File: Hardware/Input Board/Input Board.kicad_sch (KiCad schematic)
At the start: 13 parts, among them J1 Keyboard, J2 Mouse, J3 PORT A, J4 Audio L, J5 Audio R, J6 3.5mm TRS, J7 SNES Controller 1, J8 PORT B, J9 SNES Controller 2, U1 74HC595, U2 Adafruit MicroSD Breakout

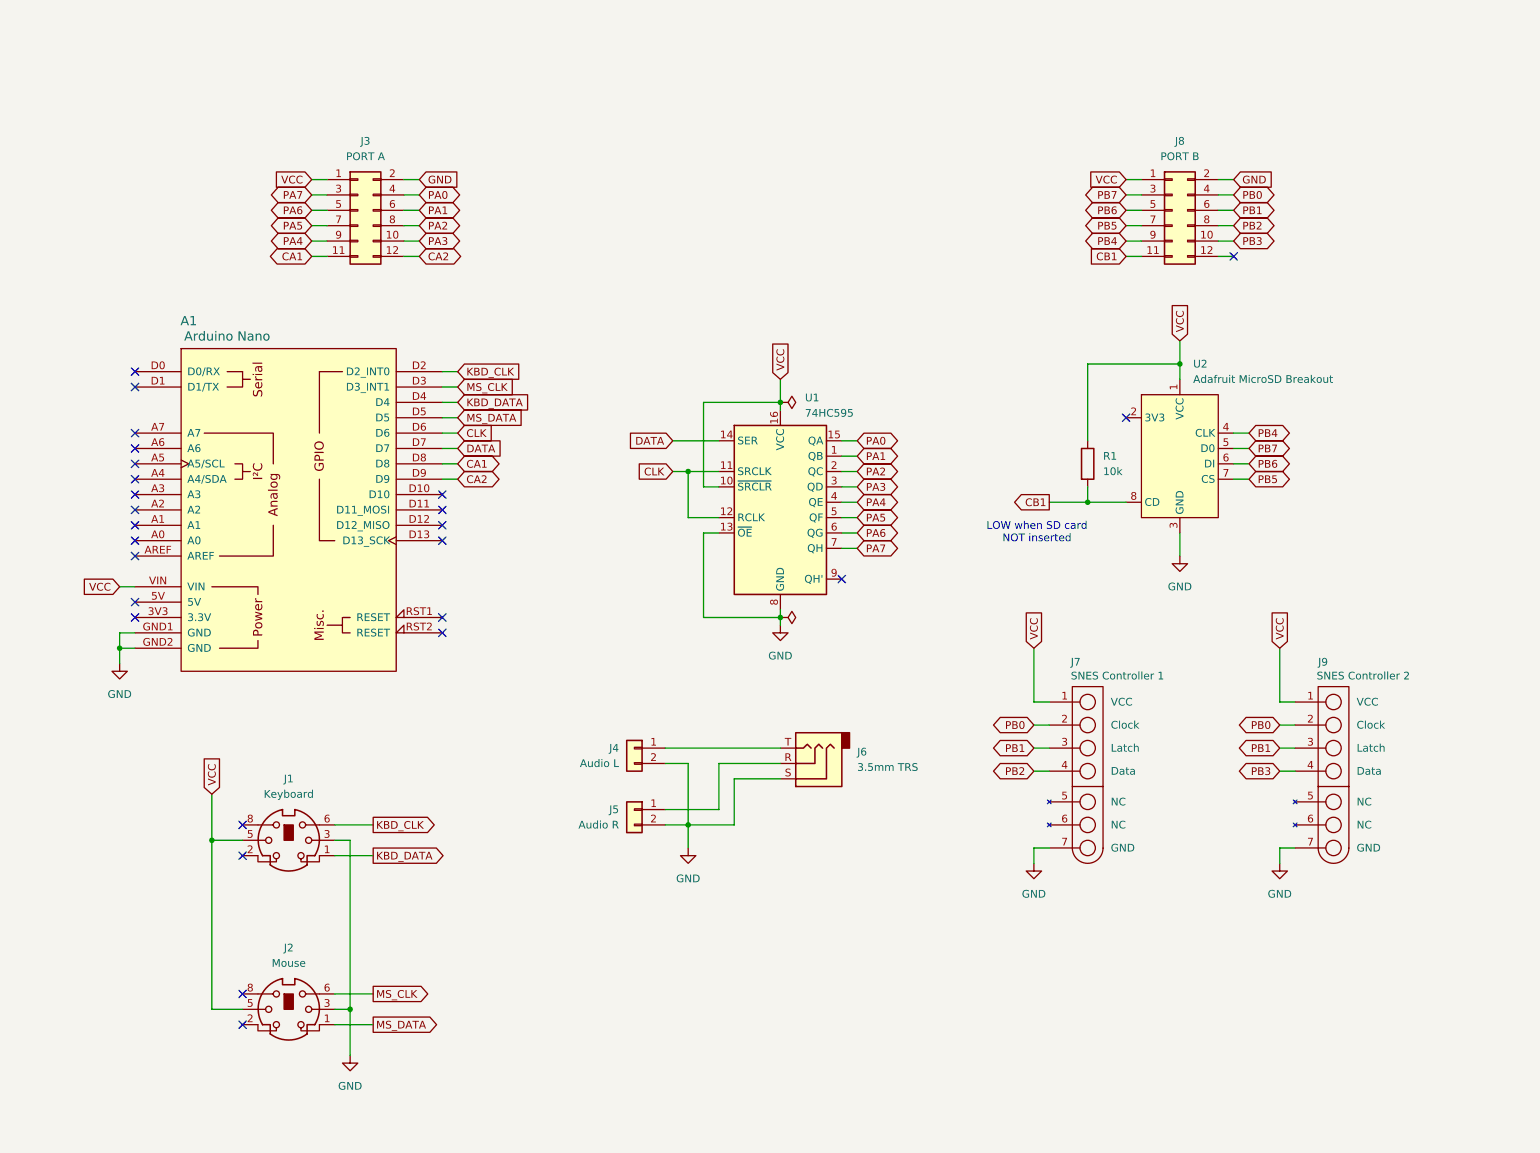
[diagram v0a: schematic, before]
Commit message: Add Input Board and rework Debugger
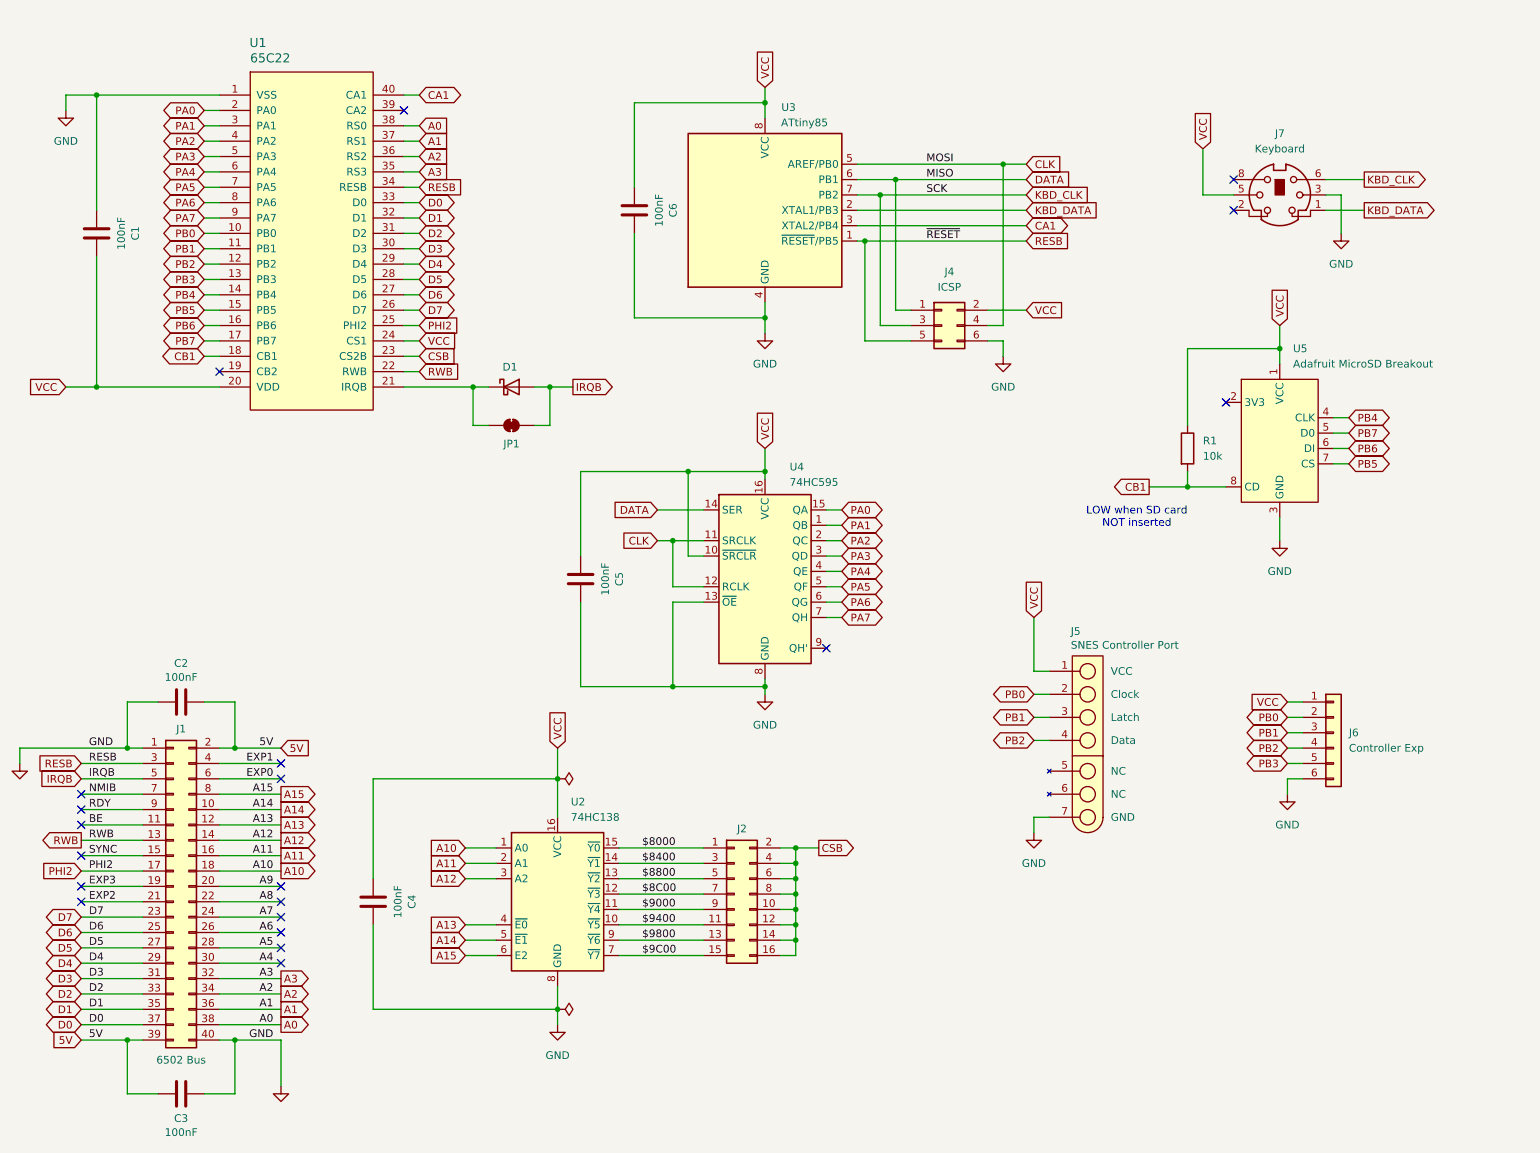
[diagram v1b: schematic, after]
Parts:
- removed A1: Arduino Nano, PCM_arduino-library:Arduino_Nano_Socket, symbol PCM_arduino-library:Arduino_Nano_Socket
- removed J2: Mouse, 6502 Parts:KMDGX-6S-BS, symbol 6502 Parts:KMDGX-6S-BS
- removed J3: PORT A, Connector_PinHeader_2.54mm:PinHeader_2x06_P2.54mm_Vertical, symbol Connector_Generic:Conn_02x06_Odd_Even
- removed J4: Audio L, Connector_JST:JST_XH_B2B-XH-A_1x02_P2.50mm_Vertical, symbol Connector_Generic:Conn_01x02
- removed J5: Audio R, Connector_JST:JST_XH_B2B-XH-A_1x02_P2.50mm_Vertical, symbol Connector_Generic:Conn_01x02
- removed J6: 3.5mm TRS, Connector_Audio:Jack_3.5mm_CUI_SJ1-3523N_Horizontal, symbol Connector_Audio:AudioJack3
- removed J8: PORT B, Connector_PinHeader_2.54mm:PinHeader_2x06_P2.54mm_Vertical, symbol Connector_Generic:Conn_02x06_Odd_Even
- removed J9: SNES Controller 2, 6502 Parts:SNES Controller Socket, symbol 6502 Parts:SNES Controller Socket
- added C1, C2, C3, C4, C5, C6: 100nF, Capacitor_SMD:C_0805_2012Metric, symbol Device:C
- added D1: D_Schottky, Diode_THT:D_DO-35_SOD27_P7.62mm_Horizontal, symbol Device:D_Schottky
- added J1: 6502 Bus, Connector_PinHeader_2.54mm:PinHeader_2x20_P2.54mm_Vertical, symbol Connector_Generic:Conn_02x20_Odd_Even
- added J2: Conn_02x08_Odd_Even, Connector_PinHeader_2.54mm:PinHeader_2x08_P2.54mm_Vertical, symbol Connector_Generic:Conn_02x08_Odd_Even
- added J4: ICSP, Connector_PinHeader_2.54mm:PinHeader_2x03_P2.54mm_Vertical, symbol Connector_Generic:Conn_02x03_Odd_Even
- added J6: Controller Exp, Connector_PinHeader_2.54mm:PinHeader_1x06_P2.54mm_Horizontal, symbol Connector_Generic:Conn_01x06
- added JP1: SolderJumper_2_Bridged, Jumper:SolderJumper-2_P1.3mm_Bridged_RoundedPad1.0x1.5mm, symbol Jumper:SolderJumper_2_Bridged
- added U1: 65C22, Package_DIP:DIP-40_W15.24mm_Socket_LongPads, symbol 6502 Parts:65C22
- added U2: 74HC138, Package_SO:SOIC-16_3.9x9.9mm_P1.27mm, symbol 74xx:74HC138
- added U3: ATtiny85, Package_DIP:DIP-8_W7.62mm_LongPads, symbol MCU_Microchip_ATtiny:ATtiny85-20P
- J5: renamed from J7; value SNES Controller 1 -> SNES Controller Port; footprint 6502 Parts:SNES Controller Socket -> 6502 Parts:SNES Controller Port; symbol 6502 Parts:SNES Controller Socket -> 6502 Parts:SNES Controller Port; now left out of the parts list
- J7: renamed from J1; now left out of the parts list
- R1: footprint Resistor_THT:R_Axial_DIN0204_L3.6mm_D1.6mm_P7.62mm_Horizontal -> Resistor_SMD:R_0805_2012Metric; LCSC (none) -> C17414
- U4: renamed from U1; footprint Package_DIP:DIP-16_W10.16mm_LongPads -> Package_SO:SOIC-16_3.9x9.9mm_P1.27mm; LCSC (none) -> C5947
- renumbered U2 to U5
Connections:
- net CA1: now also U1.40 (CA1), U3.3 (XTAL2/PB4)
- net CB1: now also U1.18 (CB1)
- net CLK: now also J4.4 (Pin_4), U3.5 (AREF/PB0)
- net DATA: now also J4.1 (Pin_1), U3.6 (PB1)
- net GND: now also C1.1, C2.2, C3.1, C4.2, C5.2, C6.2, J1.1 (Pin_1), J1.40 (Pin_40), J4.6 (Pin_6), J6.6 (Pin_6), U1.1 (VSS), U2.8 (GND), U3.4 (GND)
- net KBD_CLK: now also J4.3 (Pin_3), U3.7 (PB2)
- net KBD_DATA: now also U3.2 (XTAL1/PB3)
- net PA0: now also U1.2 (PA0)
- net PA1: now also U1.3 (PA1)
- net PA2: now also U1.4 (PA2)
- net PA3: now also U1.5 (PA3)
- net PA4: now also U1.6 (PA4)
- net PA5: now also U1.7 (PA5)
- net PA6: now also U1.8 (PA6)
- net PA7: now also U1.9 (PA7)
- net PB0: now also J6.2 (Pin_2), U1.10 (PB0)
- net PB1: now also J6.3 (Pin_3), U1.11 (PB1)
- net PB2: now also J6.4 (Pin_4), U1.12 (PB2)
- net PB3: now also J6.5 (Pin_5), U1.13 (PB3)
- net PB4: now also U1.14 (PB4)
- net PB5: now also U1.15 (PB5)
- net PB6: now also U1.16 (PB6)
- net PB7: now also U1.17 (PB7)
- net VCC: now also C1.2, C4.1, C5.1, C6.1, J4.2 (Pin_2), J6.1 (Pin_1), U1.20 (VDD), U1.24 (CS1), U2.16 (VCC), U3.8 (VCC)
- new net: D1.1 (K), JP1.1 (A), U1.21 (IRQB)
- new net $8000: J2.1 (Pin_1), U2.15 (~{Y0})
- new net $8400: J2.3 (Pin_3), U2.14 (~{Y1})
- new net $8800: J2.5 (Pin_5), U2.13 (~{Y2})
- new net $8C00: J2.7 (Pin_7), U2.12 (~{Y3})
- new net $9000: J2.9 (Pin_9), U2.11 (~{Y4})
- new net $9400: J2.11 (Pin_11), U2.10 (~{Y5})
- new net $9800: J2.13 (Pin_13), U2.9 (~{Y6})
- new net $9C00: J2.15 (Pin_15), U2.7 (~{Y7})
- new net 5V: C2.1, C3.2, J1.2 (Pin_2), J1.39 (Pin_39)
- new net A0: J1.38 (Pin_38), U1.38 (RS0)
- new net A1: J1.36 (Pin_36), U1.37 (RS1)
- new net A10: J1.18 (Pin_18), U2.1 (A0)
- new net A11: J1.16 (Pin_16), U2.2 (A1)
- new net A12: J1.14 (Pin_14), U2.3 (A2)
- new net A13: J1.12 (Pin_12), U2.4 (~{E0})
- new net A14: J1.10 (Pin_10), U2.5 (~{E1})
- new net A15: J1.8 (Pin_8), U2.6 (E2)
- new net A2: J1.34 (Pin_34), U1.36 (RS2)
- new net A3: J1.32 (Pin_32), U1.35 (RS3)
- new net A4: J1.30 (Pin_30)
- new net A5: J1.28 (Pin_28)
- new net A6: J1.26 (Pin_26)
- new net A7: J1.24 (Pin_24)
- new net A8: J1.22 (Pin_22)
- new net A9: J1.20 (Pin_20)
- new net BE: J1.11 (Pin_11)
- new net CSB: J2.10 (Pin_10), J2.12 (Pin_12), J2.14 (Pin_14), J2.16 (Pin_16), J2.2 (Pin_2), J2.4 (Pin_4), J2.6 (Pin_6), J2.8 (Pin_8), U1.23 (CS2B)
- new net D0: J1.37 (Pin_37), U1.33 (D0)
- new net D1: J1.35 (Pin_35), U1.32 (D1)
- new net D2: J1.33 (Pin_33), U1.31 (D2)
- new net D3: J1.31 (Pin_31), U1.30 (D3)
- new net D4: J1.29 (Pin_29), U1.29 (D4)
- new net D5: J1.27 (Pin_27), U1.28 (D5)
- new net D6: J1.25 (Pin_25), U1.27 (D6)
- new net D7: J1.23 (Pin_23), U1.26 (D7)
- new net EXP0: J1.6 (Pin_6)
- new net EXP1: J1.4 (Pin_4)
- new net EXP2: J1.21 (Pin_21)
- new net EXP3: J1.19 (Pin_19)
- new net IRQB: D1.2 (A), J1.5 (Pin_5), JP1.2 (B)
- new net NMIB: J1.7 (Pin_7)
- new net PHI2: J1.17 (Pin_17), U1.25 (PHI2)
- new net RDY: J1.9 (Pin_9)
- new net RESB: J1.3 (Pin_3), J4.5 (Pin_5), U1.34 (RESB), U3.1 (~{RESET}/PB5)
- new net RWB: J1.13 (Pin_13), U1.22 (RWB)
- new net SYNC: J1.15 (Pin_15)
- no-connect marks 26 -> 20
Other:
- title: 6502 Input Helper -> 6502 Input Board
- moved on the sheet: J7, R1, U4, U5

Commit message: Revise some boards
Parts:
- J1: footprint Connector_PinHeader_2.54mm:PinHeader_2x20_P2.54mm_Vertical -> 6502 Parts:6502 Bus Connector
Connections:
- net 5V is gone; now on net VCC: C2.1, C3.2, J1.2 (Pin_2), J1.39 (Pin_39)
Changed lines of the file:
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@@
 	(title_block
 		(title "6502 Input Board")
-		(date "2024-06-16")
+		(date "2024-06-19")
 		(rev "1.0")
 		(company "A.C. Wright Design")
@@
 		)
 	)
-	(label "5V"
+	(label "VCC"
 		(at 29.21 184.15 0)
 		(fields_autoplaced yes)
@@
 		)
 	)
-	(label "5V"
+	(label "VCC"
 		(at 59.69 135.89 180)
 		(fields_autoplaced yes)
@@
 		)
 	)
-	(global_label "5V"
+	(global_label "VCC"
 		(shape input)
 		(at 60.96 135.89 0)
@@
 		)
 		(property "Intersheetrefs" "${INTERSHEET_REFS}"
-			(at 66.2433 135.89 0)
+			(at 66.9196 135.89 0)
 			(effects
 				(font
@@
 		)
 	)
-	(global_label "5V"
+	(global_label "VCC"
 		(shape input)
 		(at 27.94 184.15 180)
@@
 		)
 		(property "Intersheetrefs" "${INTERSHEET_REFS}"
-			(at 22.6567 184.15 0)
+			(at 21.9804 184.15 0)
 			(effects
 				(font
@@
 			)
 		)
-		(property "Footprint" "Connector_PinHeader_2.54mm:PinHeader_2x20_P2.54mm_Vertical"
+		(property "Footprint" "6502 Parts:6502 Bus Connector"
 			(at 43.18 158.75 0)
 			(effects

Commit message: Working on schematics
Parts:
- removed J4: ICSP, Connector_PinHeader_2.54mm:PinHeader_2x03_P2.54mm_Vertical, symbol Connector_Generic:Conn_02x03_Odd_Even
- removed J6: Controller Exp, Connector_PinHeader_2.54mm:PinHeader_1x06_P2.54mm_Horizontal, symbol Connector_Generic:Conn_01x06
- removed U5: Adafruit MicroSD Breakout, 6502 Parts:Adafruit MicroSD Breakout, symbol 6502 Parts:Adafruit MicroSD Breakout
- added C7: 100nF, Capacitor_SMD:C_0805_2012Metric, symbol Device:C
- added D2, D3: D_Schottky, Diode_THT:D_DO-35_SOD27_P7.62mm_Horizontal, symbol Device:D_Schottky
- added J2: PORT B, 6502 Parts:6502 GPIO Connector, symbol Connector_Generic:Conn_02x06_Odd_Even
- added J6: Mouse, 6502 Parts:KMDGX-6S-BS, symbol 6502 Parts:KMDGX-6S-BS
- added J7: SNES Controller Port 2, 6502 Parts:SNES Controller Port, symbol 6502 Parts:SNES Controller Port
- added U5: ATtiny85, Package_DIP:DIP-8_W7.62mm_LongPads, symbol MCU_Microchip_ATtiny:ATtiny85-20P
- J4: renamed from J5; value SNES Controller Port -> SNES Controller Port 1
- renumbered J2 to J3, J7 to J5, U4 to U3, U3 to U4
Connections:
- net CB1: now also J2.11 (Pin_11); no longer R1.2
- net CLK: now also U5.5 (AREF/PB0)
- net DATA: now also U5.6 (PB1)
- net GND: now also R1.2, C7.2, J2.2 (Pin_2), J6.3, J7.7 (GND), U5.4 (GND)
- net PB0: now also J2.4 (Pin_4), J7.2 (Clock)
- net PB1: now also J2.6 (Pin_6), J7.3 (Latch)
- net PB2: now also J2.8 (Pin_8)
- net PB3: now also J2.10 (Pin_10), J7.4 (Data)
- net PB4: now also J2.9 (Pin_9)
- net PB5: now also J2.7 (Pin_7)
- net PB6: now also J2.5 (Pin_5)
- net PB7: now also J2.3 (Pin_3)
- net RESB: no longer U4.1 (~{RESET}/PB5)
- net VCC: now also C7.1, J2.1 (Pin_1), J6.5, J7.1 (VCC), U5.8 (VCC); no longer R1.1
- net CB2: now reaches U1.19 (CB2)
- net CB2: now also J2.12 (Pin_12)
- net CA2: now reaches U1.39 (CA2)
- net CA2: now also U4.1 (~{RESET}/PB5), U5.1 (~{RESET}/PB5)
- net CA1: no longer names the net of U1.40 (CA1)
- net CA1: now also R1.1, D2.1 (K), D3.1 (K); no longer U4.3 (XTAL2/PB4)
- new net KBD_INT: D2.2 (A), U4.3 (XTAL2/PB4)
- new net MS_CLK: J6.6, U5.7 (PB2)
- new net MS_DATA: J6.1, U5.2 (XTAL1/PB3)
- new net MS_INT: D3.2 (A), U5.3 (XTAL2/PB4)
- no-connect marks 20 -> 19
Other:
- note removed: "LOW when SD card NOT inserted"
- moved on the sheet: C4, C5, C6, J3, J4, J5, U2, U3, U4
